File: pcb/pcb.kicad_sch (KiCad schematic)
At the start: 37 parts, among them J1 USB_C_Receptacle_USB2.0_14P, J2 Conn_01x20, J3 Conn_01x20, J4 Conn_01x03, SW1 SW_Push, U1 RP2040, U2 MCP1700x-330xxTT, U3 W25Q16JVZPIQ, Y1 12 MHz

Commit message: holy shit massive update the pcb routing is done
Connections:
- net GPIO8: now also J2.11 (Pin_11)
- net GPIO9: now also J2.12 (Pin_12)
- no-connect marks 5 -> 3
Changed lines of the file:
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@@
 		(at 254 93.98)
 	)
-	(no_connect
-		(at 31.75 140.97)
-	)
-	(no_connect
-		(at 31.75 138.43)
+	(wire
+		(pts
+			(xy 27.94 140.97) (xy 31.75 140.97)
+		)
+		(stroke
+			(width 0)
+			(type default)
+		)
 	)
 	(wire
@@
 		(pts
 			(xy 74.93 125.73) (xy 81.28 125.73)
+		)
+		(stroke
+			(width 0)
+			(type default)
+		)
+	)
+	(wire
+		(pts
+			(xy 27.94 138.43) (xy 31.75 138.43)
 		)
 		(stroke
@@
 		)
 	)
+	(global_label "GPIO8"
+		(shape bidirectional)
+		(at 27.94 138.43 180)
+		(fields_autoplaced yes)
+		(effects
+			(font
+				(size 1.27 1.27)
+			)
+			(justify right)
+		)
+		(property "Intersheetrefs" "${INTERSHEET_REFS}"
+			(at 18.1587 138.43 0)
+			(effects
+				(font
+					(size 1.27 1.27)
+				)
+				(justify right)
+				(hide yes)
+			)
+		)
+	)
 	(global_label "GPIO22"
 		(shape bidirectional)
@@
 				(hide yes)
 			)
+		)
+	)
+	(global_label "GPIO9"
+		(shape bidirectional)
+		(at 27.94 140.97 180)
+		(fields_autoplaced yes)
+		(effects
+			(font
+				(size 1.27 1.27)
+			)
+			(justify right)
+		)
+		(property "Intersheetrefs" "${INTERSHEET_REFS}"
+			(at 18.1587 140.97 0)
+			(effects
+				(font
+					(size 1.27 1.27)
+				)
+				(justify right)
+				(hide yes)
+			)

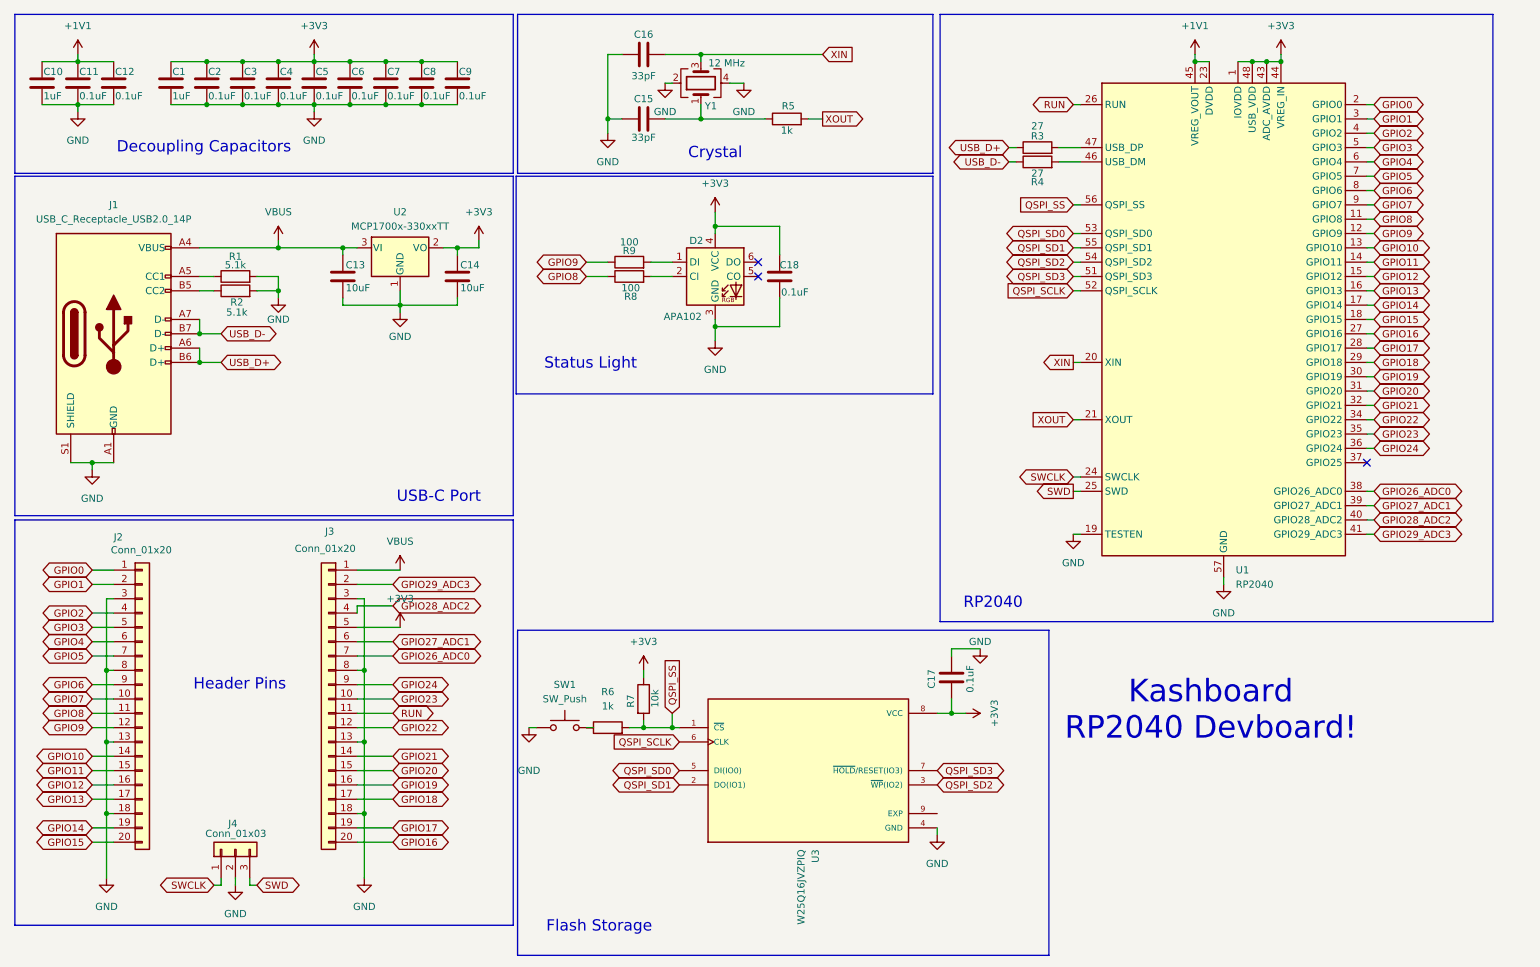
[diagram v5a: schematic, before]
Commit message: replaced the apa102 with sk6182 neopixel
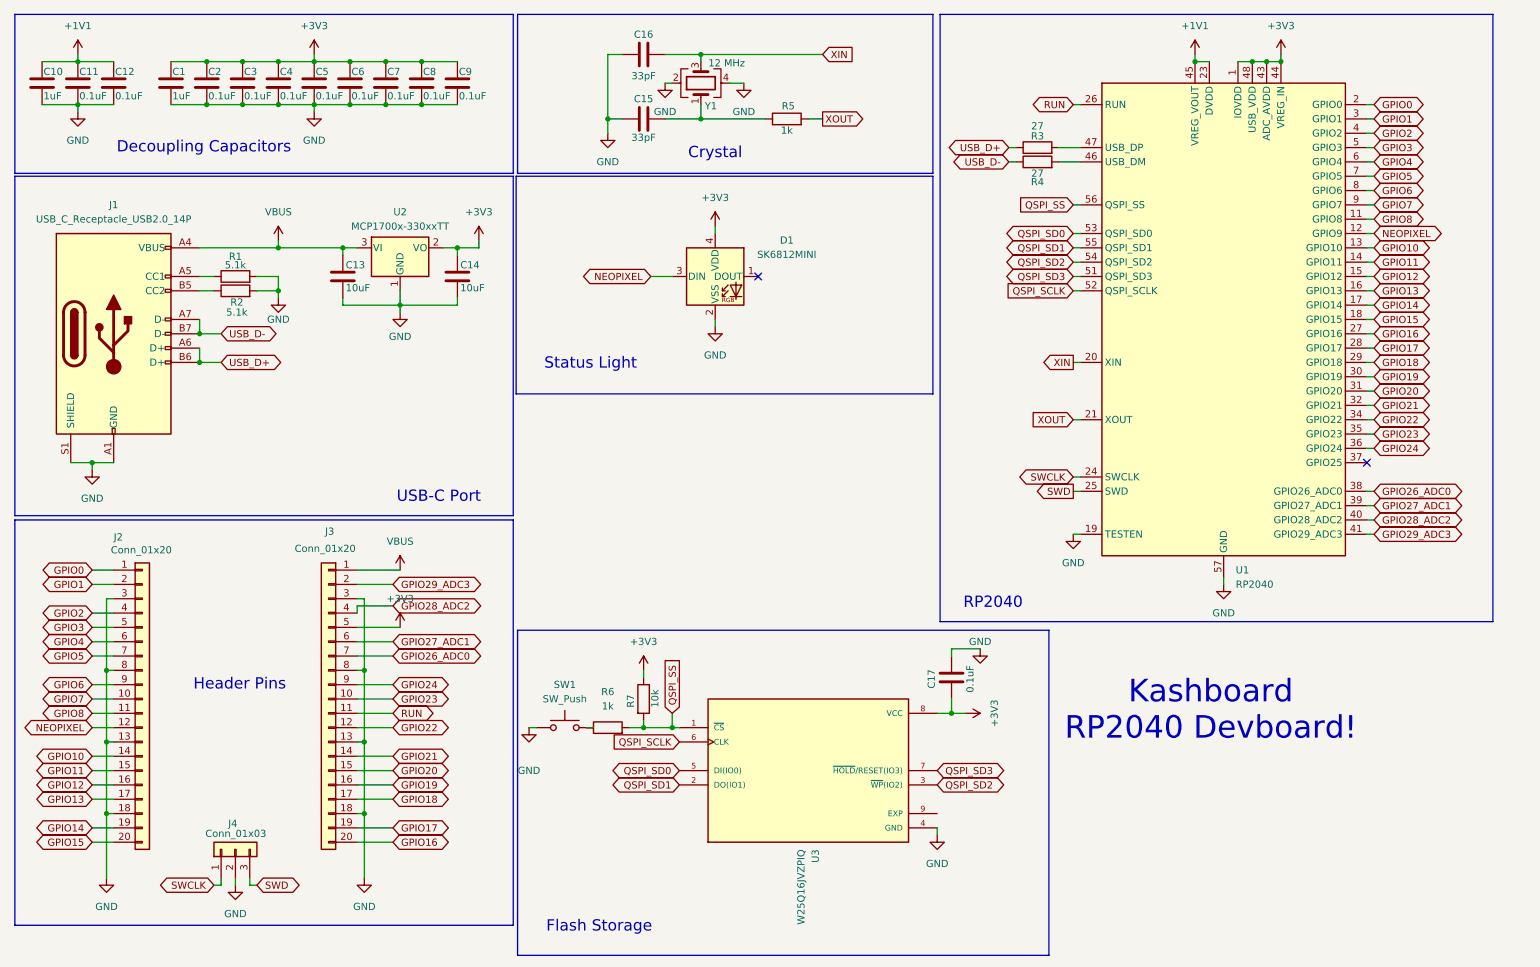
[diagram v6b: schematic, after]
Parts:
- removed C18: 0.1uF, Capacitor_SMD:C_0402_1005Metric, symbol Device:C
- removed D2: APA102, LED_SMD:LED_RGB_5050-6, symbol LED:APA102
- removed R8, R9: 100, Resistor_SMD:R_0402_1005Metric, symbol Device:R
- added D1: SK6812MINI, LED_SMD:LED_SK6812MINI_PLCC4_3.5x3.5mm_P1.75mm, symbol LED:SK6812MINI
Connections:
- net +3V3: now also D1.4 (VDD)
- net GND: now also D1.2 (VSS)
- net GPIO9 renamed NEOPIXEL
- net NEOPIXEL: now also D1.3 (DIN)
- no-connect marks 3 -> 2
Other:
- company: (none) -> Kashyap Sukshavasi
- title: (none) -> Kashboard
